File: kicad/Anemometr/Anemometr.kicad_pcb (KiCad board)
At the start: 2 copper layers, 44.9 x 45.2 mm, 168 parts, among them J1 +5.5v, J10 +Z3, J11 -Z3, J12 +Z4, J13 -Z4, J14 SWD, J15 SWC, J16 Z4, J17 Z4, J18 1 TxD+, J19 2 TxD-, J2 Conn_01x01_Female, J20 3 RxD+, J21 4, J22 5, J23 6 RxD-, J24 7, J25 8, J26 Z4, J27 Z4, J28 Z4, J29 Z4, J3 RST, J30 Z4, J31 Z4, J32 Z4, J33 Z4, J34 Z4, J35 Z4, J4 TxD, J5 RxD, J6 +Z1, J7 -Z1, J8 +Z2, J9 -Z2, Q1 5N10, U1 TS5A3166DBVR, U10 MCP1700-3002E, U2 LMV7239, U3 TS5A3166DBVR, U4 TS5A3166DBVR, U5 STM32F103C8Tx, U6 TS5A3166DBVR, U7 LM2734Y, U8 MCP1700-5002E, U9 MCP1700-3002E, Y1 8MHz, Y2 25MHz

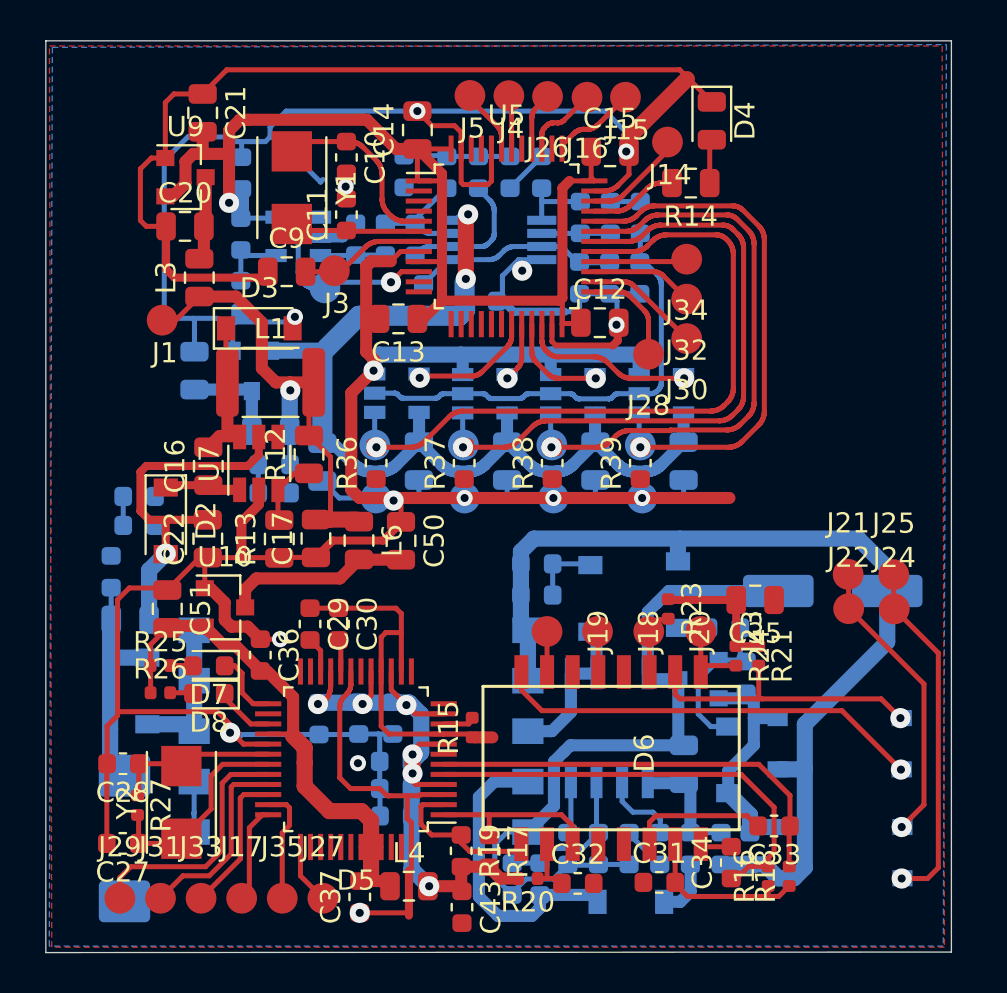
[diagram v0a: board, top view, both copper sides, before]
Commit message: новый файл:    Documents/boardA.png 	новый файл:    Documents/boardB.png 	изменено:      Documents/circuit.png 	изменено:      kicad/Anemometr/Anemometr.kicad_pcb 	изменено:      kicad/Anemometr/Anemometr.kicad_pcb-bak 	изменено:      kicad/Anemometr/Anemometr.pdf 	изменено:      kicad/Anemometr/Anemometr.sch 	изменено:      kicad/Anemometr/Anemometr.sch-bak 	изменено:      stm32cubeide/Anemometer/.cproject 	изменено:      stm32cubeide/Anemometer/.mxproject 	изменено:      stm32cubeide/Anemometer/Anemometer.ioc 	изменено:      stm32cubeide/Anemometer/Core/Inc/main.h 	изменено:      stm32cubeide/Anemometer/Core/Inc/stm32f1xx_hal_conf.h 	изменено:      stm32cubeide/Anemometer/Core/Src/main.c 	изменено:      stm32cubeide/Anemometer/Core/Src/stm32f1xx_hal_msp.c 	изменено:      stm32cubeide/Anemometer/Release/Anemometer.bin 	изменено:      stm32cubeide/Anemometer/Release/Anemometer.elf 	изменено:      stm32cubeide/Anemometer/Release/Anemometer.list 	изменено:      stm32cubeide/Anemometer/Release/Anemometer.map 	изменено:      stm32cubeide/Anemometer/Release/Core/Src/main.d 	изменено:      stm32cubeide/Anemometer/Release/Core/Src/main.o 	изменено:      stm32cubeide/Anemometer/Release/Core/Src/main.su 	изменено:      stm32cubeide/Anemometer/Release/Core/Src/stm32f1xx_hal_msp.d 	изменено:      stm32cubeide/Anemometer/Release/Core/Src/stm32f1xx_hal_msp.o 	изменено:      stm32cubeide/Anemometer/Release/Core/Src/stm32f1xx_hal_msp.su 	изменено:      stm32cubeide/Anemometer/Release/Core/Src/stm32f1xx_it.d 	изменено:      stm32cubeide/Anemometer/Release/Core/Src/system_stm32f1xx.d 	изменено:      stm32cubeide/Anemometer/Release/Drivers/STM32F1xx_HAL_Driver/Src/stm32f1xx_hal.d 	изменено:      stm32cubeide/Anemometer/Release/Drivers/STM32F1xx_HAL_Driver/Src/stm32f1xx_hal_cortex.d 	изменено:      stm32cubeide/Anemometer/Release/Drivers/STM32F1xx_HAL_Driver/Src/stm32f1xx_hal_dma.d 	изменено:      stm32cubeide/Anemometer/Release/Drivers/STM32F1xx_HAL_Driver/Src/stm32f1xx_hal_exti.d 	и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
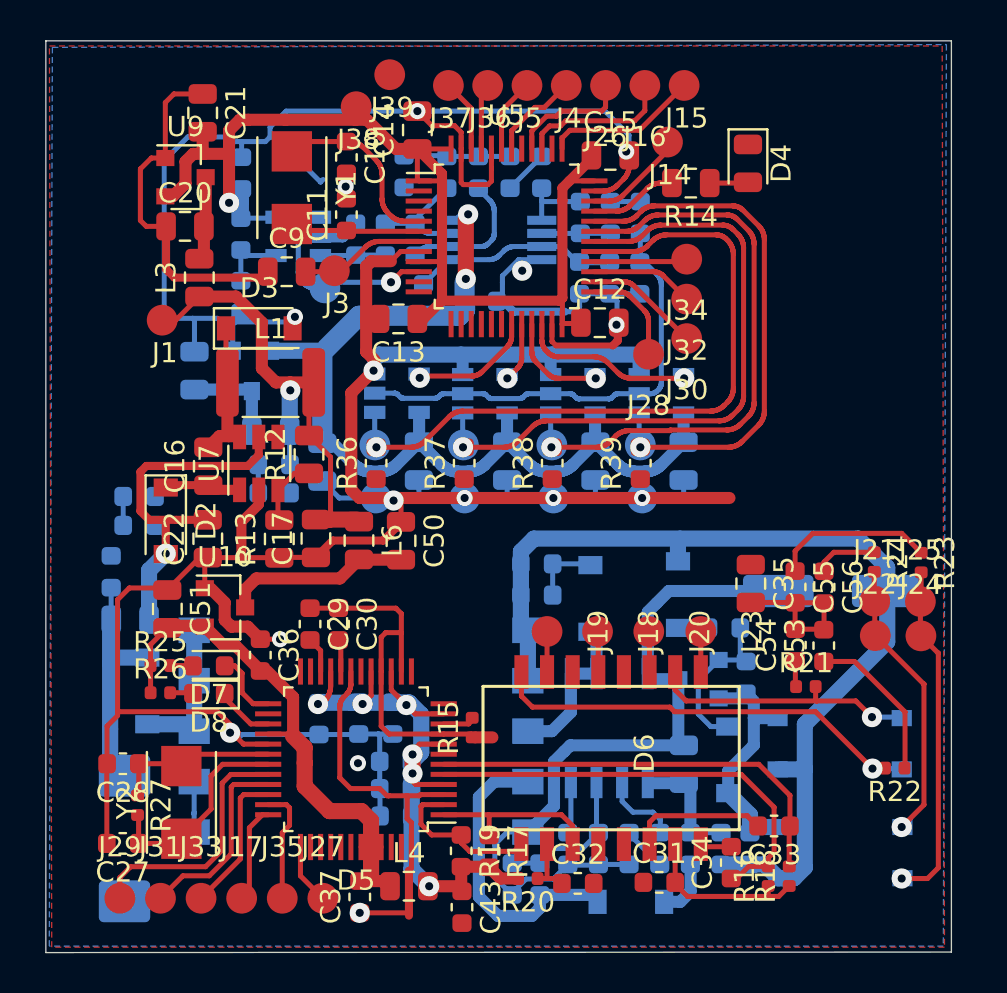
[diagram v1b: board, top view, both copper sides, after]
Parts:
- added C53: 6.8nF, Capacitor_SMD:C_0603_1608Metric, F.Cu at (57.4, 89.6)
- added C54: 6.8nF, Capacitor_SMD:C_0603_1608Metric, F.Cu at (56.0, 89.5)
- added C55: 6.8nF, Capacitor_SMD:C_0603_1608Metric, F.Cu at (56.0, 86.7)
- added C56: 6.8nF, Capacitor_SMD:C_0603_1608Metric, F.Cu at (57.4, 86.7)
- added J36: TMP117, My-library:SMD-CONN, F.Cu at (40.8, 61.8)
- added J37: TMP117, My-library:SMD-CONN, F.Cu at (38.8, 61.8)
- added J38: TMP117, My-library:SMD-CONN, F.Cu at (34.3, 62.9)
- added J39: TMP117, My-library:SMD-CONN, F.Cu at (35.9, 61.3)
- added R22: 75, Resistor_SMD:R_0402_1005Metric, F.Cu at (60.9, 95.6)
- R21: value 75R -> 75
- R23, R24: value 150R -> 75
- moved R23 12.7 mm to (62.3, 85.5)
- moved R24 8.28 mm to (59.9, 85.4)
- moved J15 2.97 mm to (50.5, 61.8)
- moved J26 2.93 mm to (46.6, 61.8)
- moved J16 2.92 mm to (48.6, 61.8)
- moved J4 2.89 mm to (44.7, 61.8)
- moved J5 2.87 mm to (42.7, 61.8)
- moved R21 2.79 mm to (56.5, 91.6), turned to 0 degrees
- moved D4 2.77 mm to (53.7, 65.7)
- moved J22 1.88 mm to (60.0, 89.1)
- moved J21 1.88 mm to (60.0, 87.4)
- moved J24 1.88 mm to (62.2, 89.1)
- moved J25 1.88 mm to (62.2, 87.4)
- moved C35 0.84 mm to (53.8, 86.5), turned to 270 degrees
- moved C15 0.18 mm to (46.9, 65.3)
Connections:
- R21 pad 1: Net-(C35-Pad2) -> Net-(C54-Pad1)
- R23 pad 1: Net-(C35-Pad2) -> Net-(C55-Pad1)
- R23 pad 2: Net-(D6-Pad11) -> Net-(D10-Pad2)
- R24 pad 1: Net-(C35-Pad2) -> Net-(C56-Pad1)
- R24 pad 2: Net-(D6-Pad9) -> Net-(D10-Pad1)
- U5 pad 45: (no net) -> Net-(J36-Pad1)
- U5 pad 46: (no net) -> Net-(J37-Pad1)
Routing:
- net GND: track 303.5 -> 271.9 mm
- net Net-(C55-Pad1): track 0.00 -> 8.00 mm
- net Net-(C53-Pad1): track 0.00 -> 7.85 mm
- net Net-(J16-Pad1): track 3.76 -> 7.57 mm
- net Net-(J37-Pad1): track 0.00 -> 3.60 mm
- net Net-(J15-Pad1): track 4.23 -> 7.65 mm
- net Net-(J36-Pad1): track 0.00 -> 3.26 mm
- net Net-(J26-Pad1): track 2.88 -> 6.10 mm
- net Net-(C56-Pad1): track 0.00 -> 3.15 mm
- net Net-(D6-Pad9): track 3.88 -> 2.00 mm
- net Net-(J4-Pad1): track 2.68 -> 4.53 mm
- net Net-(C54-Pad1): track 0.00 -> 1.28 mm
- net Net-(D6-Pad11): track 3.23 -> 2.01 mm
- net Net-(C35-Pad2): track 6.60 -> 7.70 mm
- net Net-(D6-Pad10): track 14.4 -> 13.4 mm
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
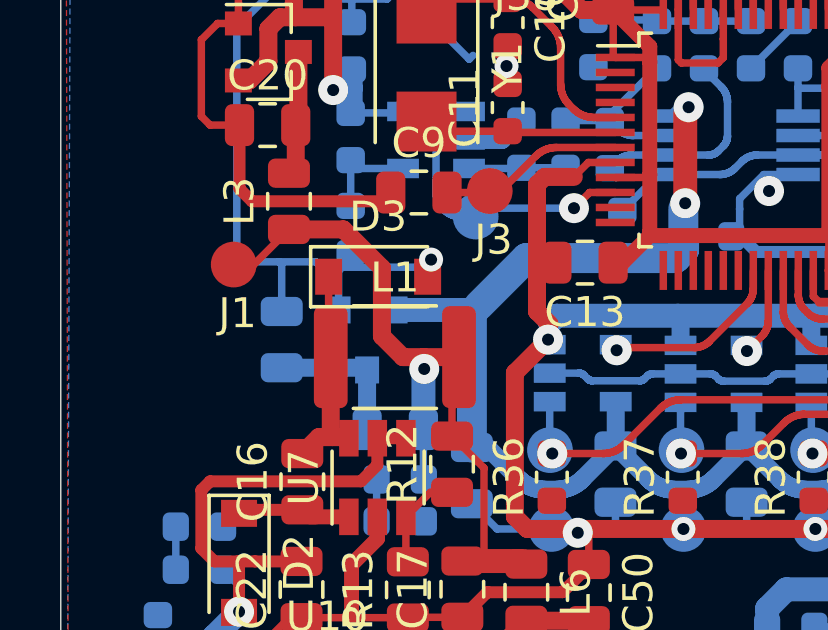
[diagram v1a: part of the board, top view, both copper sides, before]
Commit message: изменено:      kicad/Anemometr/Anemometr.kicad_pcb 	изменено:      kicad/Anemometr/Anemometr.kicad_pcb-bak 	изменено:      kicad/Anemometr/Anemometr.sch 	изменено:      kicad/Anemometr/Anemometr.sch-bak 	изменено:      kicad/Anemometr/fp-info-cache 	изменено:      stm32cubeide/Anemometer/Anemometer.ioc 	изменено:      stm32cubeide/Anemometer/Core/Src/main.c 	изменено:      stm32cubeide/Anemometer/Release/Anemometer.bin 	изменено:      stm32cubeide/Anemometer/Release/Anemometer.elf 	изменено:      stm32cubeide/Anemometer/Release/Anemometer.list 	изменено:      stm32cubeide/Anemometer/Release/Core/Src/main.o
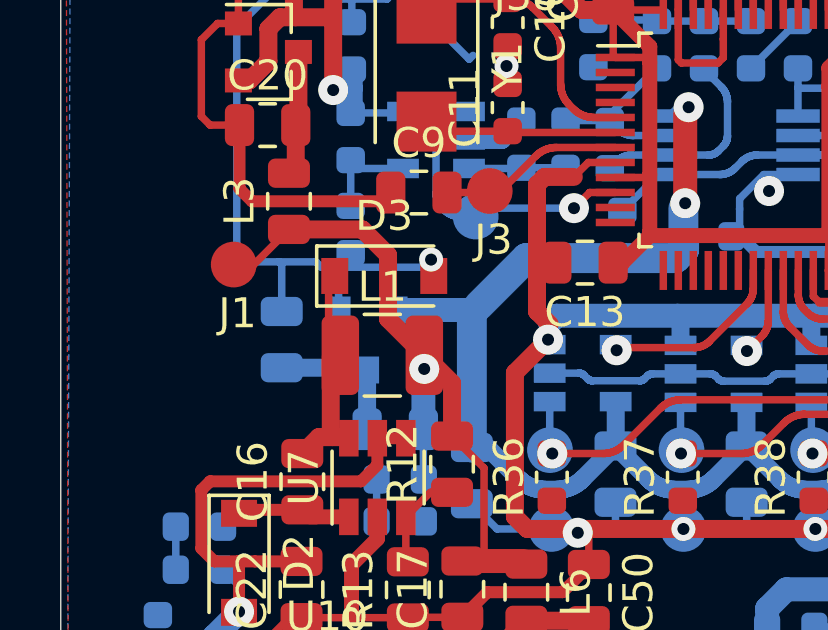
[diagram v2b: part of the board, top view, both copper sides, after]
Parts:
- L1: footprint Inductor_SMD:L_1812_4532Metric -> Inductor_SMD:L_1210_3225Metric
- R12: value 100k -> 56k
- R29: value 43k -> 30k
- moved L1 0.42 mm to (29.6, 76.5)
- moved D3 0.20 mm to (29.7, 73.8)
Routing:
- net Net-(C17-Pad2): track 24.7 -> 23.8 mm

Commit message: изменено:      kicad/Anemometr/Anemometr.kicad_pcb 	изменено:      kicad/Anemometr/Anemometr.kicad_pcb-bak 	изменено:      kicad/Anemometr/Anemometr.sch 	изменено:      kicad/Anemometr/Anemometr.sch-bak 	изменено:      kicad/Anemometr/fp-info-cache 	изменено:      stm32cubeide/Anemometer/.cproject 	изменено:      stm32cubeide/Anemometer/.mxproject 	изменено:      stm32cubeide/Anemometer/.project 	изменено:      stm32cubeide/Anemometer/Anemometer.ioc 	изменено:      stm32cubeide/Anemometer/Core/Inc/main.h 	изменено:      stm32cubeide/Anemometer/Core/Inc/stm32f1xx_hal_conf.h 	новый файл:    stm32cubeide/Anemometer/Core/Inc/w5500.h 	новый файл:    stm32cubeide/Anemometer/Core/Inc/wizchip_conf.h 	новый файл:    stm32cubeide/Anemometer/Core/Src/dhcp.c 	новый файл:    stm32cubeide/Anemometer/Core/Src/dns.c 	изменено:      stm32cubeide/Anemometer/Core/Src/main.c 	новый файл:    stm32cubeide/Anemometer/Core/Src/socket.c 	изменено:      stm32cubeide/Anemometer/Core/Src/stm32f1xx_hal_msp.c 	новый файл:    stm32cubeide/Anemometer/Core/Src/w5500.c 	новый файл:    stm32cubeide/Anemometer/Core/Src/wizchip_conf.c 	удалено:       stm32cubeide/Anemometer/Drivers/STM32F1xx_HAL_Driver/Inc/stm32f1xx_hal_spi.h 	удалено:       stm32cubeide/Anemometer/Drivers/STM32F1xx_HAL_Driver/Src/stm32f1xx_hal_spi.c 	изменено:      stm32cubeide/Anemometer/Release/Anemometer.bin 	изменено:      stm32cubeide/Anemometer/Release/Anemometer.elf 	изменено:      stm32cubeide/Anemometer/Release/Anemometer.list 	изменено:      stm32cubeide/Anemometer/Release/Anemometer.map 	изменено:      stm32cubeide/Anemometer/Release/Core/Src/main.d 	изменено:      stm32cubeide/Anemometer/Release/Core/Src/main.o 	изменено:      stm32cubeide/Anemometer/Release/Core/Src/main.su 	изменено:      stm32cubeide/Anemometer/Release/Core/Src/stm32f1xx_hal_msp.d 	изменено:      stm32cubeide/Anemometer/Release/Core/Src/stm32f1xx_hal_msp.o 	изменено:      stm32cubeide/Anemometer/Release/Core/Src/stm32f1xx_hal_msp.su 	изменено:      stm3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
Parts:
- removed J1: +5.5v, My-library:SMD-CONN
- removed J16, J17, J26, J27, J28, J29, J30, J31, J32, J33, J34, J35: Z4, My-library:SMD-CONN
- removed J22: 5, My-library:SMD-CONN
- removed J25: 8, My-library:SMD-CONN
- C36, L4: moved to B.Cu
- C9: footprint Capacitor_SMD:C_0805_2012Metric -> Capacitor_SMD:C_0603_1608Metric
- D18, D19: footprint LED_SMD:LED_0603_1608Metric -> LED_SMD:LED_0805_2012Metric
- J21: value 4 -> 4-5
- J24: value 7 -> 7-8
- R15, R16, R18, R20, R21, R22, R23, R24, R25, R26: footprint Resistor_SMD:R_0402_1005Metric -> Resistor_SMD:R_0603_1608Metric
- moved D18 41.4 mm to (60.3, 101.3)
- moved R35 41.2 mm to (61.2, 99.0), turned to 270 degrees
- moved J24 41.1 mm to (21.3, 86.1)
- moved C49 40.1 mm to (60.6, 85.8), turned to 90 degrees
- moved C27 39.5 mm to (60.4, 87.8), turned to 0 degrees
- moved R22 39.0 mm to (22.1, 91.5)
- moved R43 39.0 mm to (59.3, 99.0), turned to 90 degrees
- moved J21 38.7 mm to (21.3, 88.7)
- moved R23 38.4 mm to (23.9, 86.5), turned to 180 degrees
- moved L5 38.2 mm to (60.3, 96.6), turned to 0 degrees
- moved C28 37.9 mm to (60.4, 91.7), turned to 0 degrees
- moved R27 37.1 mm to (59.7, 89.6), turned to 90 degrees
- moved R24 36.5 mm to (23.6, 88.8), turned to 180 degrees
- moved D10 36.1 mm to (24.4, 87.4), turned to 0 degrees
- moved C45 35.8 mm to (24.8, 100.4), turned to 0 degrees
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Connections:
- D5 pad 36: Net-(D5-Pad36) -> (no net)
- D9 pad 1: Net-(D6-Pad10) -> Net-(D6-Pad15)
- D9 pad 2: Net-(D6-Pad15) -> Net-(D6-Pad10)
- R21 pad 2: Net-(D6-Pad10) -> Net-(D6-Pad15)
- R22 pad 2: Net-(D6-Pad15) -> Net-(D6-Pad10)
- U5 pad 25: Net-(J28-Pad1) -> Net-(D5-Pad32)
- U5 pad 26: Net-(J30-Pad1) -> Net-(D5-Pad33)
- U5 pad 27: Net-(J32-Pad1) -> Net-(D5-Pad34)
- U5 pad 28: Net-(J34-Pad1) -> Net-(D5-Pad35)
- U5 pad 39: Net-(J16-Pad1) -> (no net)
- U5 pad 40: Net-(J26-Pad1) -> Net-(D5-Pad37)
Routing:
- net Net-(C22-Pad2): track 20.5 -> 71.7 mm
- net Net-(D5-Pad37): track 3.00 -> 41.0 mm
- net Net-(D5-Pad35): track 5.75 -> 34.3 mm, vias 0 -> 2
- net Net-(D5-Pad34): track 7.22 -> 33.8 mm, vias 0 -> 2
- net Net-(D5-Pad33): track 9.62 -> 33.4 mm, vias 0 -> 2
- net Net-(D5-Pad32): track 12.4 -> 33.1 mm, vias 0 -> 2
- net Net-(C34-Pad1): track 22.2 -> 5.43 mm
- net Net-(C33-Pad1): track 21.3 -> 5.30 mm
- net Net-(D10-Pad2): track 17.1 -> 1.98 mm
- net Net-(D10-Pad1): track 14.2 -> 1.54 mm
- net Net-(D5-Pad2): track 7.96 -> 19.3 mm, vias 0 -> 2
- net Net-(D6-Pad15): track 22.2 -> 11.2 mm
- net Net-(C31-Pad2): track 8.63 -> 16.5 mm
- net Net-(J16-Pad1): track 7.57 -> 0.00 mm
- net Net-(D5-Pad1): track 8.56 -> 15.2 mm, vias 0 -> 2
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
